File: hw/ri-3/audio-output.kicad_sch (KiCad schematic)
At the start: 17 parts, among them U91 TLV9152

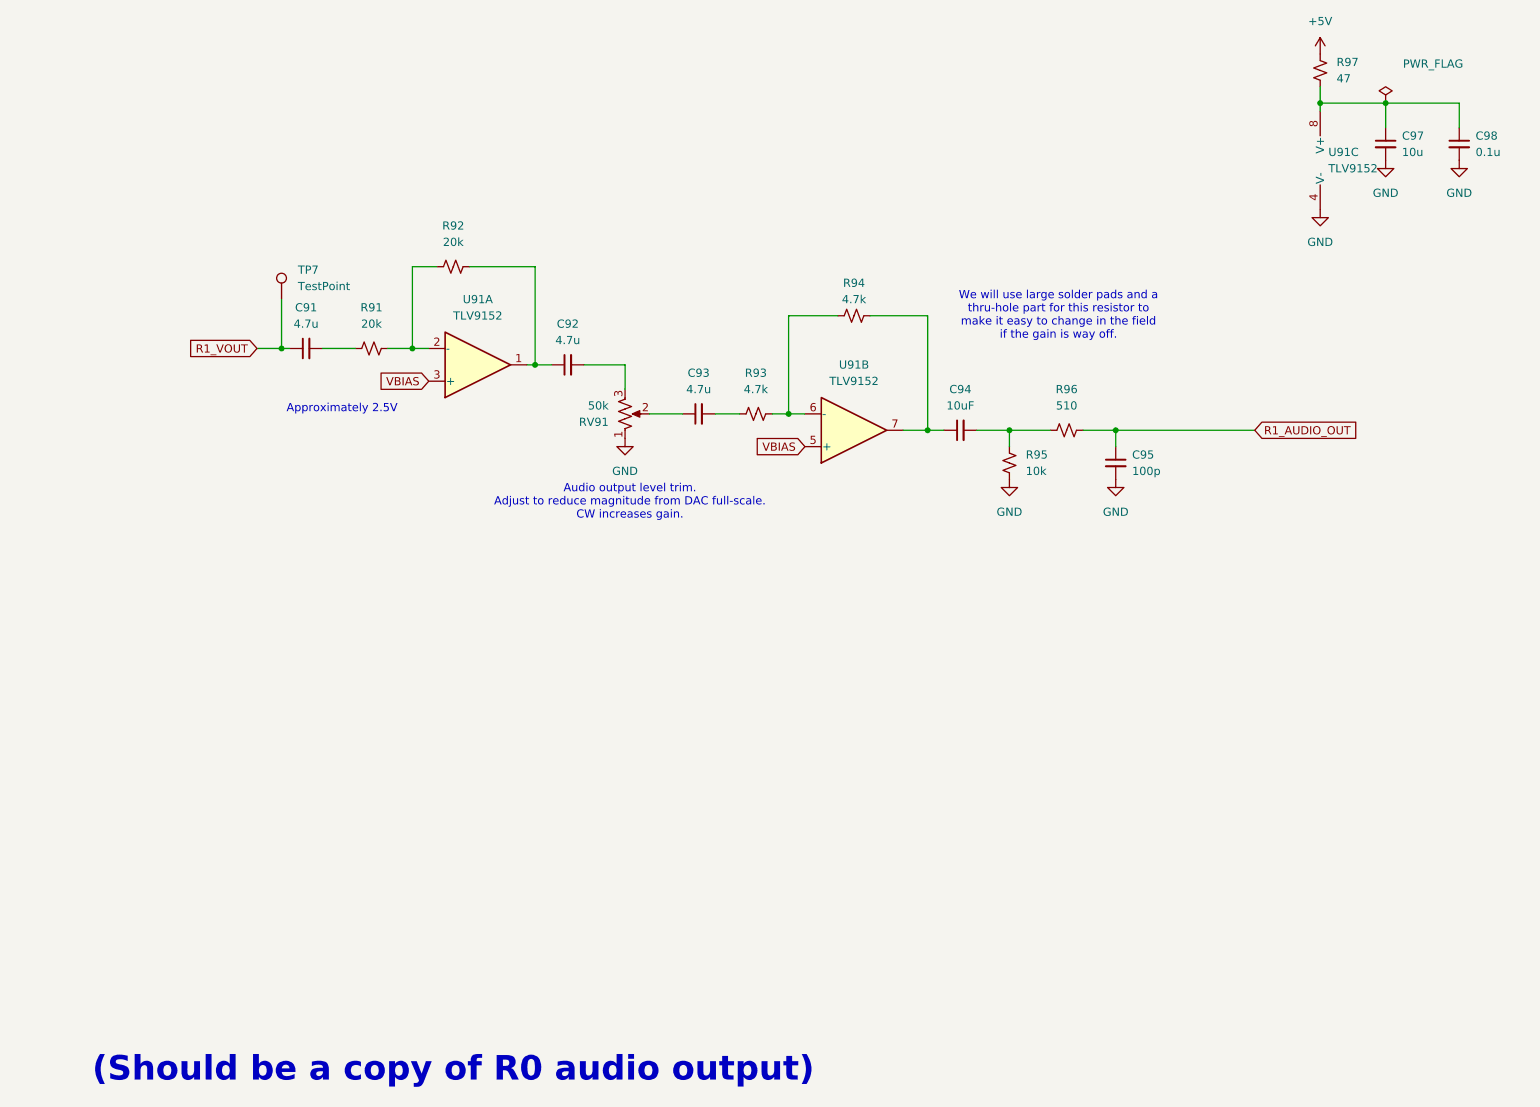
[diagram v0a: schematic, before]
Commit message: Updating schematics, create new mini-board for radio interface
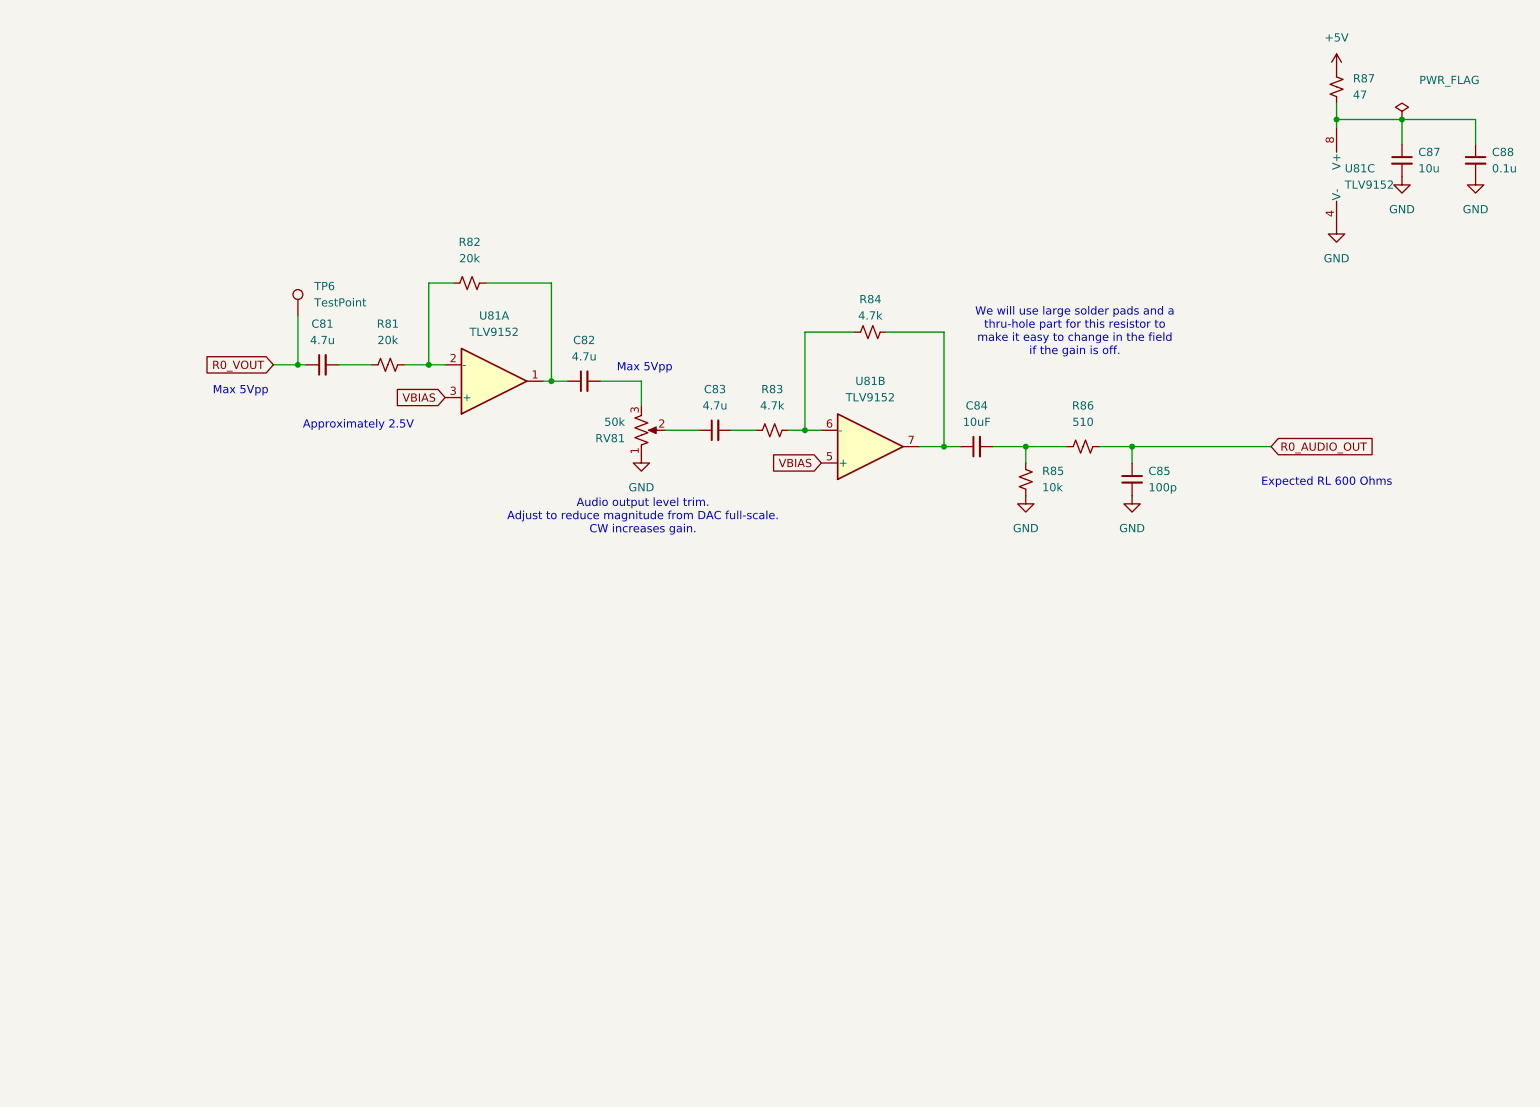
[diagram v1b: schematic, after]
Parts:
- removed C91, C92, C93: 4.7u, Capacitor_SMD:C_0805_2012Metric_Pad1.18x1.45mm_HandSolder, symbol Device:C_Small
- removed C94: 10uF, Capacitor_SMD:C_0805_2012Metric_Pad1.18x1.45mm_HandSolder, symbol Device:C_Small
- removed C95: 100p, Capacitor_SMD:C_0805_2012Metric_Pad1.18x1.45mm_HandSolder, symbol Device:C_Small
- removed C97: 10u, Capacitor_SMD:C_0805_2012Metric_Pad1.18x1.45mm_HandSolder, symbol Device:C_Small
- removed C98: 0.1u, Capacitor_SMD:C_0805_2012Metric_Pad1.18x1.45mm_HandSolder, symbol Device:C_Small
- removed R91, R92: 20k, Resistor_SMD:R_0805_2012Metric_Pad1.20x1.40mm_HandSolder, symbol Device:R_Small_US
- removed R93: 4.7k, Resistor_SMD:R_0805_2012Metric_Pad1.20x1.40mm_HandSolder, symbol Device:R_Small_US
- removed R94: 4.7k, Resistor_THT:R_Axial_DIN0516_L15.5mm_D5.0mm_P5.08mm_Vertical, symbol Device:R_Small_US
- removed R95: 10k, Resistor_SMD:R_0805_2012Metric_Pad1.20x1.40mm_HandSolder, symbol Device:R_Small_US
- removed R96: 510, Resistor_SMD:R_0805_2012Metric_Pad1.20x1.40mm_HandSolder, symbol Device:R_Small_US
- removed R97: 47, Resistor_SMD:R_0805_2012Metric_Pad1.20x1.40mm_HandSolder, symbol Device:R_Small_US
- removed RV91: 50k, bruce-footprints:POT_3362P, symbol Device:R_Potentiometer_US
- removed TP7: TestPoint, TestPoint:TestPoint_Pad_2.5x2.5mm, symbol Connector:TestPoint
- removed U91: TLV9152, Package_SO:SOIC-8_3.9x4.9mm_P1.27mm, symbol Amplifier_Operational:TL072
- added C81, C82, C83: 4.7u, Capacitor_SMD:C_0805_2012Metric_Pad1.18x1.45mm_HandSolder, symbol Device:C_Small
- added C84: 10uF, Capacitor_SMD:C_0805_2012Metric_Pad1.18x1.45mm_HandSolder, symbol Device:C_Small
- added C85: 100p, Capacitor_SMD:C_0805_2012Metric_Pad1.18x1.45mm_HandSolder, symbol Device:C_Small
- added C87: 10u, Capacitor_SMD:C_0805_2012Metric_Pad1.18x1.45mm_HandSolder, symbol Device:C_Small
- added C88: 0.1u, Capacitor_SMD:C_0805_2012Metric_Pad1.18x1.45mm_HandSolder, symbol Device:C_Small
- added R81, R82: 20k, Resistor_SMD:R_0805_2012Metric_Pad1.20x1.40mm_HandSolder, symbol Device:R_Small_US
- added R83: 4.7k, Resistor_SMD:R_0805_2012Metric_Pad1.20x1.40mm_HandSolder, symbol Device:R_Small_US
- added R84: 4.7k, Resistor_THT:R_Axial_DIN0516_L15.5mm_D5.0mm_P5.08mm_Vertical, symbol Device:R_Small_US
- added R85: 10k, Resistor_SMD:R_0805_2012Metric_Pad1.20x1.40mm_HandSolder, symbol Device:R_Small_US
- added R86: 510, Resistor_SMD:R_0805_2012Metric_Pad1.20x1.40mm_HandSolder, symbol Device:R_Small_US
- added R87: 47, Resistor_SMD:R_0805_2012Metric_Pad1.20x1.40mm_HandSolder, symbol Device:R_Small_US
- added RV81: 50k, bruce-footprints:POT_3362P, symbol Device:R_Potentiometer_US
- added TP6: TestPoint, TestPoint:TestPoint_Pad_2.5x2.5mm, symbol Connector:TestPoint
- added U81: TLV9152, Package_SO:SOIC-8_3.9x4.9mm_P1.27mm, symbol Amplifier_Operational:TL072
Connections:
- net +5V: now also R87.2
- net GND: now also C85.2, C87.2, C88.2, R85.2, RV81.1, U81.4 (V-)
- net VBIAS: now also U81.3 (+), U81.5 (+)
- new net: C81.2, R81.1
- new net: C87.1, C88.1, R87.1, U81.8 (V+)
- new net: C83.1, RV81.2
- new net: C82.2, RV81.3
- new net: R81.2, R82.1, U81.2 (-)
- new net: C82.1, R82.2, U81.1
- new net: C84.2, R85.1, R86.1
- new net: R83.2, R84.1, U81.6 (-)
- new net: C84.1, R84.2, U81.7
- new net: C83.2, R83.1
- new net R0_AUDIO_OUT: C85.1, R86.2
- new net R0_VOUT: C81.1, TP6.1
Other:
- note added: "Expected RL 600 Ohms"
- note added: "Max 5Vpp"
- note added: "We will use large solder pads and a thru-hole part for this resistor to make it easy to change in the field if the gain is off."
- note removed: "(Should be a copy of R0 audio output)"
- note removed: "We will use large solder pads and a thru-hole part for this resistor to make it easy to change in the field if the gain is way off."
- company: Bruce MacKinnon KC1FSZ -> (none)
- title: Audio Output (Radio 1) -> (none)
